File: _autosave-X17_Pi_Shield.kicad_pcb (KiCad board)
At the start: 4 copper layers, 85 x 56 mm, 91 parts, among them J1 BM04B-GHS-TBT, J10 BM04B-GHS-TBT, J11 BM04B-GHS-TBT, J12 Conn_01x05_Pin, J13 Conn_01x03_Pin, J2 BM02B-GHS-TBT, J20 Conn_01x02_Pin, J22 430450212, J23 430450612, J24 430450212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

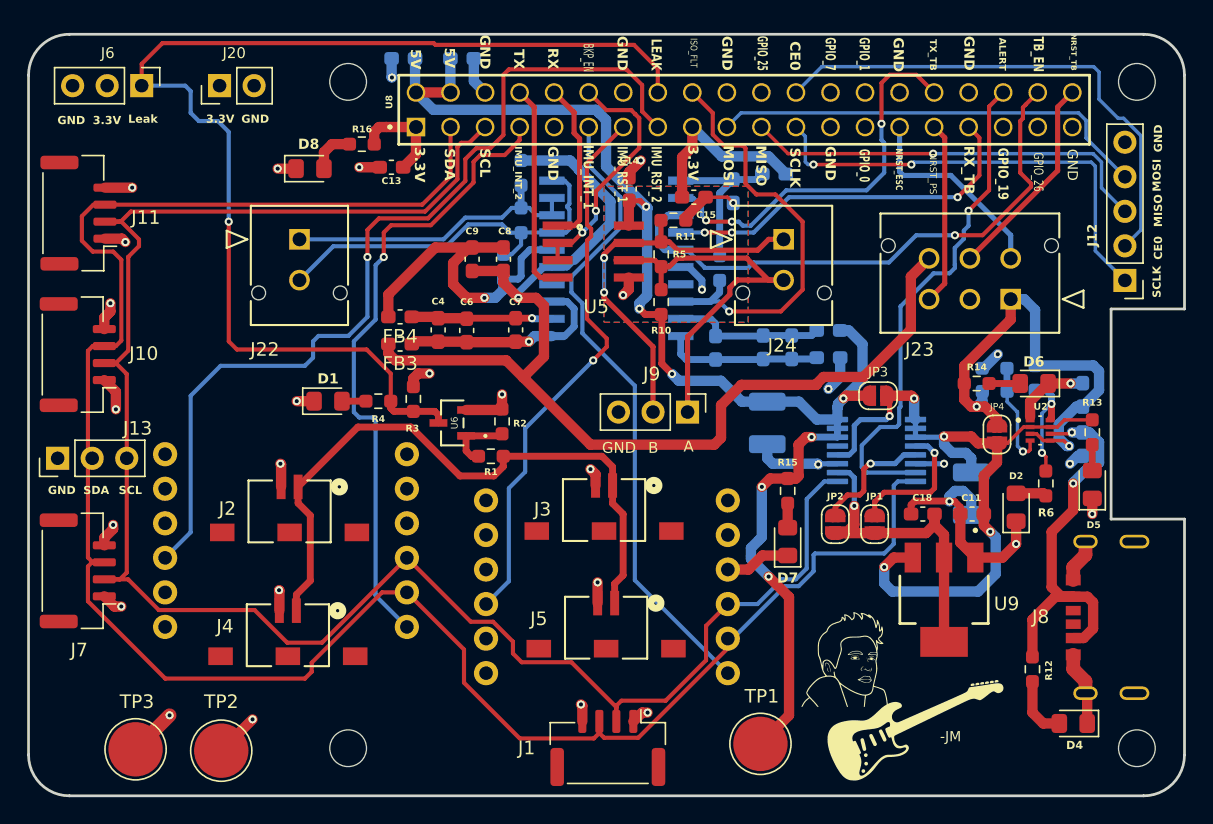
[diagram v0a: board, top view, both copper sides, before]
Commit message: fixed several DRC errors and ferrite bead package size, still reviewing the board
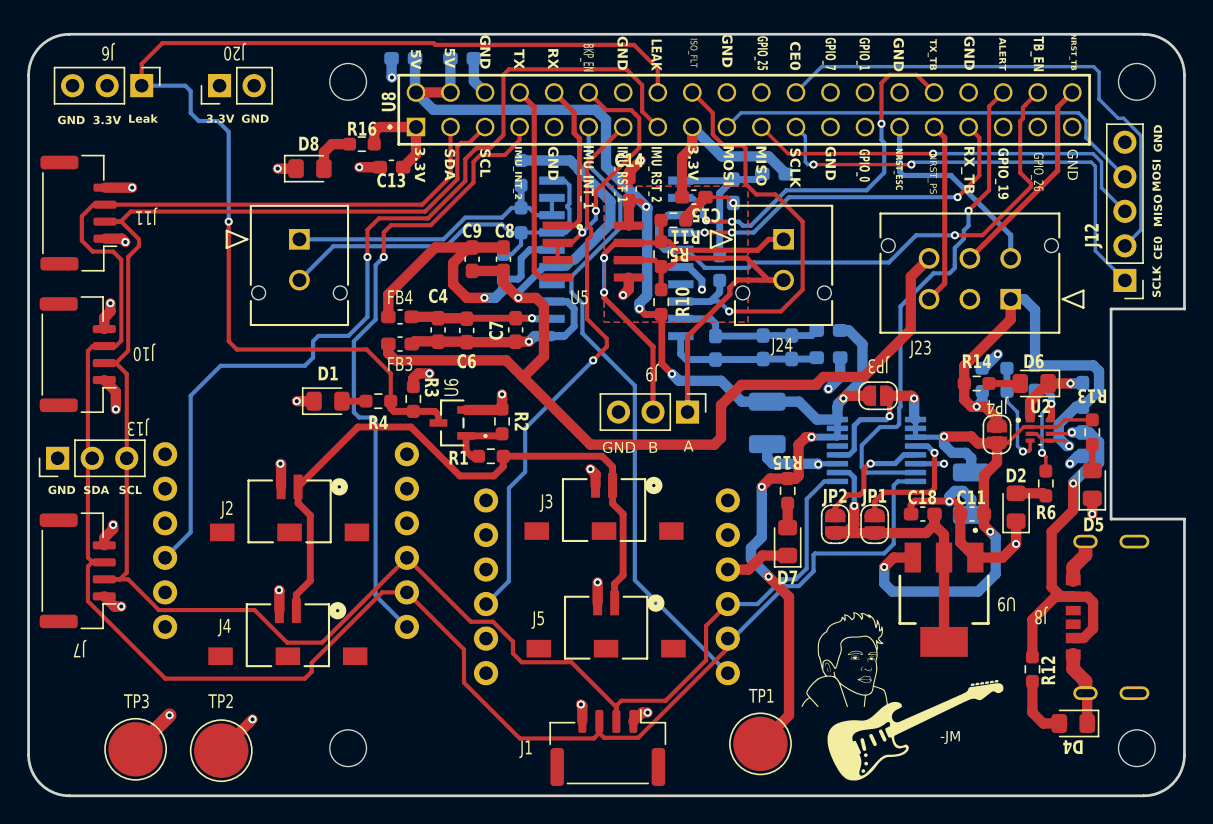
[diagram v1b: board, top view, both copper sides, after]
